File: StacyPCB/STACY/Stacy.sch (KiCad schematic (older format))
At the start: 48 parts, among them J1 SOL, J10 kill, J11 ext3, J12 push_start, J13 relays, J14 door_lock, J15 ble_hm-10, J16 door_nano, J4 ext4, J5 ext0, J6 ext1, J7 USB_B_Micro, J8 SWD Debug, J9 ext2, SW1 SW_Push, U1 ATSAMD21G18A-AUT, U2 TPS62163DSG, Y1 16MHz

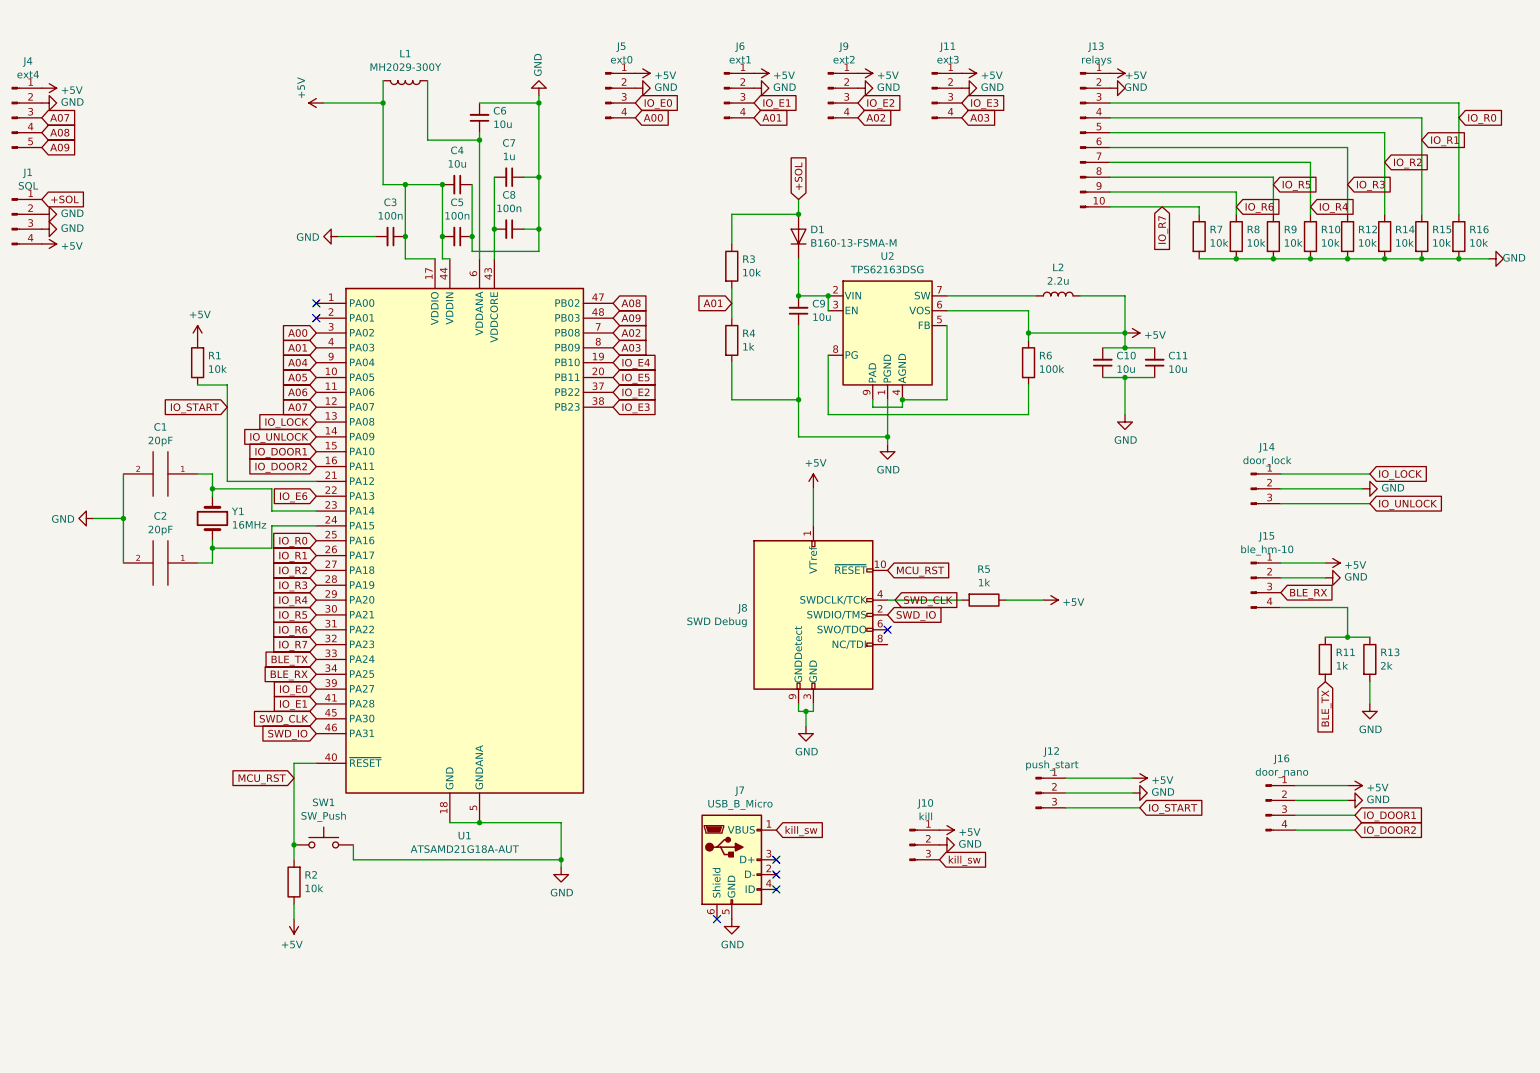
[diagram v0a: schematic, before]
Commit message: Routed all decoupling caps and fixed clock footprint. This version has been manufactured
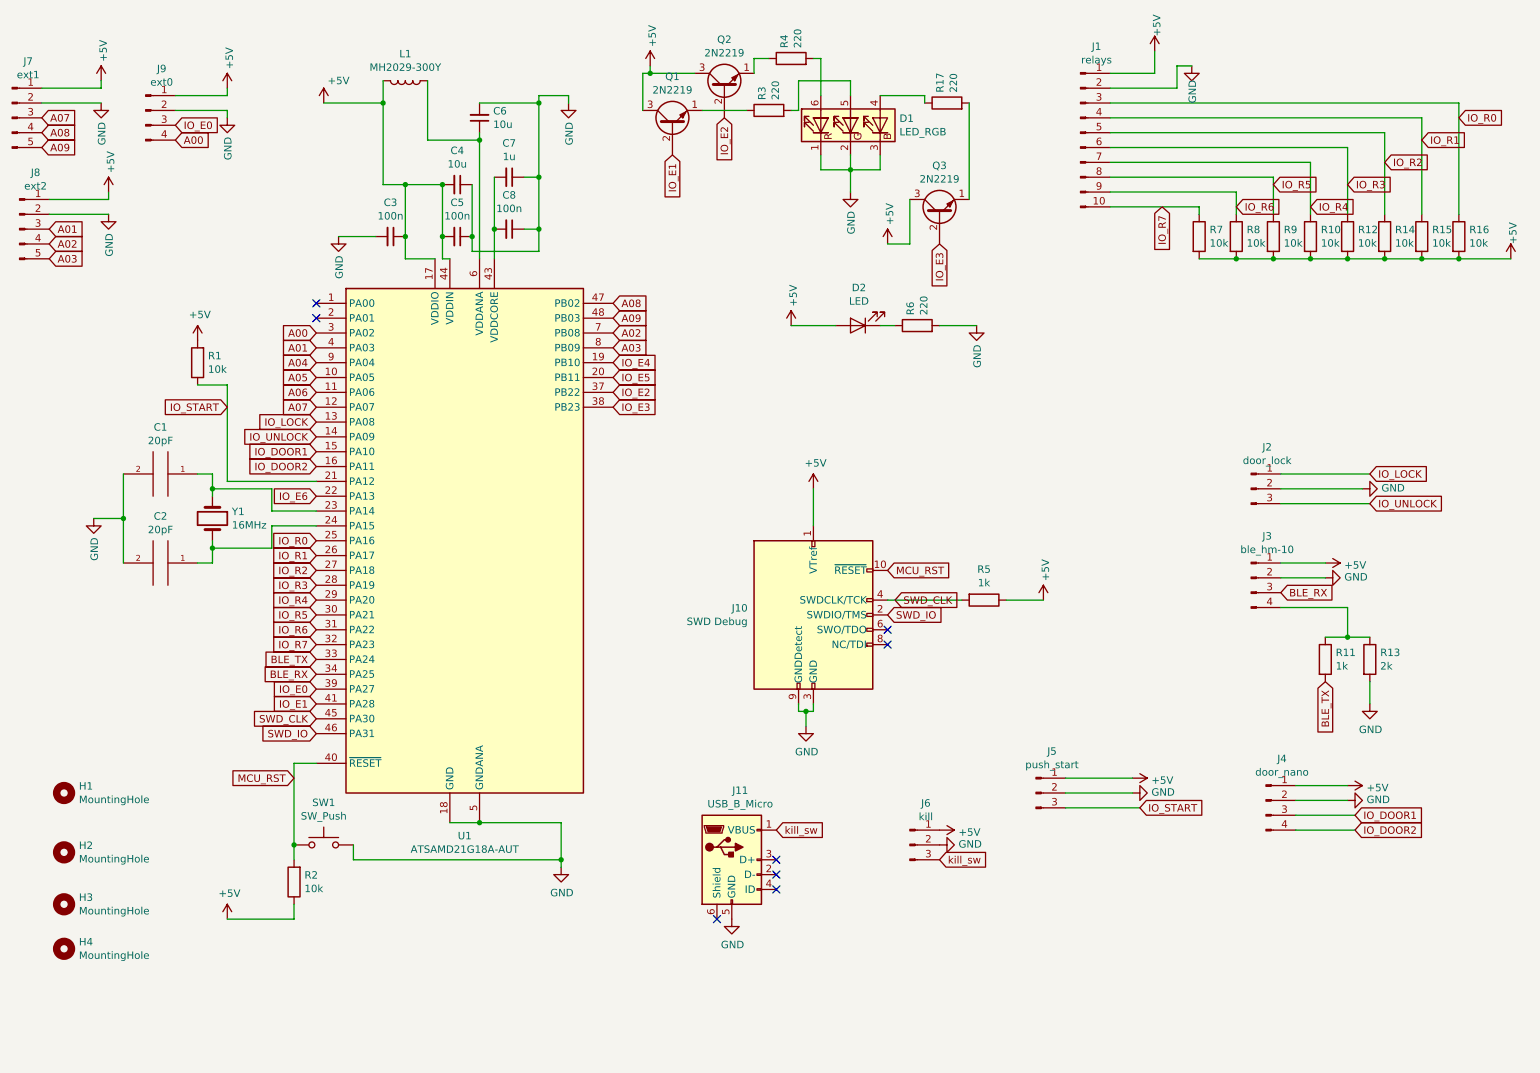
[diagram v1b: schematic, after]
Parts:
- removed C10, C11, C9: 10u, Capacitor_SMD:C_0402_1005Metric, symbol Device:C_Small
- removed D1: B160-13-FSMA-M, Diode_SMD:D_SMA, symbol Device:D
- removed J1: SOL, Connector_JST:JST_EH_B4B-EH-A_1x04_P2.50mm_Vertical, symbol Connector:Conn_01x04_Male
- removed J11: ext3, Connector_JST:JST_EH_B4B-EH-A_1x04_P2.50mm_Vertical, symbol Connector:Conn_01x04_Male
- removed J6: ext1, Connector_JST:JST_EH_B4B-EH-A_1x04_P2.50mm_Vertical, symbol Connector:Conn_01x04_Male
- removed J9: ext2, Connector_JST:JST_EH_B4B-EH-A_1x04_P2.50mm_Vertical, symbol Connector:Conn_01x04_Male
- removed L2: 2.2u, Inductor_SMD:L_0805_2012Metric, symbol Device:L
- removed U2: TPS62163DSG, Package_SON:WSON-8-1EP_2x2mm_P0.5mm_EP0.9x1.6mm_ThermalVias, symbol Regulator_Switching:TPS62163DSG
- added D1: LED_RGB, LED_SMD:LED_RGB_PLCC-6, symbol Device:LED_RGB
- added D2: LED, LED_SMD:LED_0603_1608Metric, symbol Device:LED
- added H1, H2, H3, H4: MountingHole, MountingHole:MountingHole_2.5mm, symbol Mechanical:MountingHole
- added J8: ext2, Connector_JST:JST_EH_B5B-EH-A_1x05_P2.50mm_Vertical, symbol Connector:Conn_01x05_Male
- added Q1, Q2, Q3: 2N2219, Package_TO_SOT_SMD:TSOT-23, symbol Transistor_BJT:2N2219
- added R17: 220, Resistor_SMD:R_0402_1005Metric, symbol Device:R
- J11: renamed from J7; footprint Connector_USB:USB_Micro-B_Molex-105017-0001 -> Connector_USB:USB_Micro-B_Molex_47346-0001
- J7: renamed from J4; value ext4 -> ext1
- R3: value 10k -> 220
- R4: value 1k -> 220
- R6: value 100k -> 220
- Y1: footprint Crystal:Resonator-2Pin_W6.0mm_H3.0mm -> Crystal:Crystal_HC49-U_Vertical
- renumbered J13 to J1, J8 to J10, J14 to J2, J15 to J3, J16 to J4, J12 to J5, J10 to J6, J5 to J9
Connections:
- net +5V: now also R10.2, R12.2, R14.2, R15.2, R16.2, R7.2, R8.2, R9.2, D2.2 (A), J8.1 (Pin_1), Q1.3 (C), Q2.3 (C), Q3.3 (C); no longer R6.1
- net A01: now also J8.3 (Pin_3); no longer R3.2, R4.1
- net A02: now also J8.4 (Pin_4)
- net A03: now also J8.5 (Pin_5)
- net GND: now also R6.2, D1.1 (RK), D1.2 (GK), D1.3 (BK), J8.2 (Pin_2); no longer R10.2, R12.2, R14.2, R15.2, R16.2, R4.2, R7.2, R8.2, R9.2
- net IO_E1: now also Q1.2 (B)
- net IO_E2: now also Q2.2 (B)
- net IO_E3: now also Q3.2 (B)
- net +SOL: no longer names the net of R3.1
- net +SOL: now also Q1.1 (E)
- new net: D1.4 (BA), R17.1
- new net: D1.5 (GA), R3.2
- new net: D1.6 (RA), R4.2
- new net: Q2.1 (E), R4.1
- new net: Q3.1 (E), R17.2
- new net: D2.1 (K), R6.1
- no-connect marks 7 -> 8
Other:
- moved on the sheet: J9

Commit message: fixed transistor
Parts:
- removed Q1, Q2, Q3: 2N2219, Package_TO_SOT_SMD:TSOT-23, symbol Transistor_BJT:2N2219
- added Q? (x3): Q_NMOS_GSD, TO_SOT_Packages_SMD:SOT-23, symbol Device:Q_NMOS_GSD
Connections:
- wire segments 150 -> 133
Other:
- moved on the sheet: D1, D2, R17, R3, R4, R6
